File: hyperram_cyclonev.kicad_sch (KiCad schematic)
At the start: 57 parts, among them IC1 AP63205WU, IC2 TXB0108PWR, IC3 S26KL128SDABHI020, IC4 W25Q32JVSSIQ_TR, IC5 S27KL0641DABHI020, J1 ASP-122952-01, J2 HDMI_A, J3 Conn_02x10_Odd_Even, J4 Conn_02x10_Odd_Even, J5 Conn_02x06_Odd_Even, J6 Conn_02x06_Odd_Even, J7 Conn_02x06_Odd_Even, Q1 BSS138, Q2 BSS138

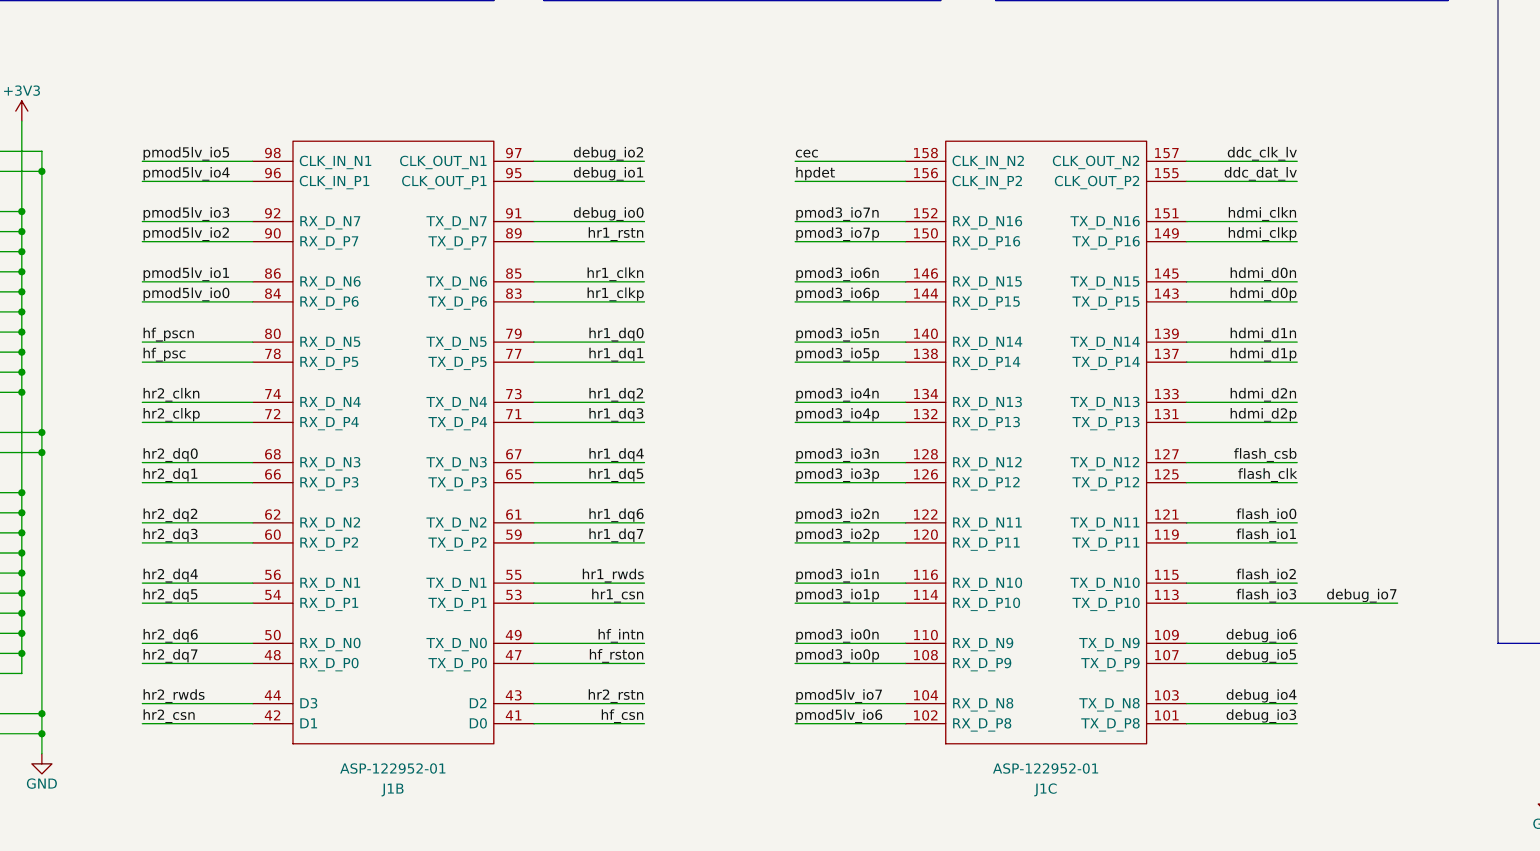
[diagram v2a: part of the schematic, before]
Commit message: Rearrange signals assignments to simplify routing.
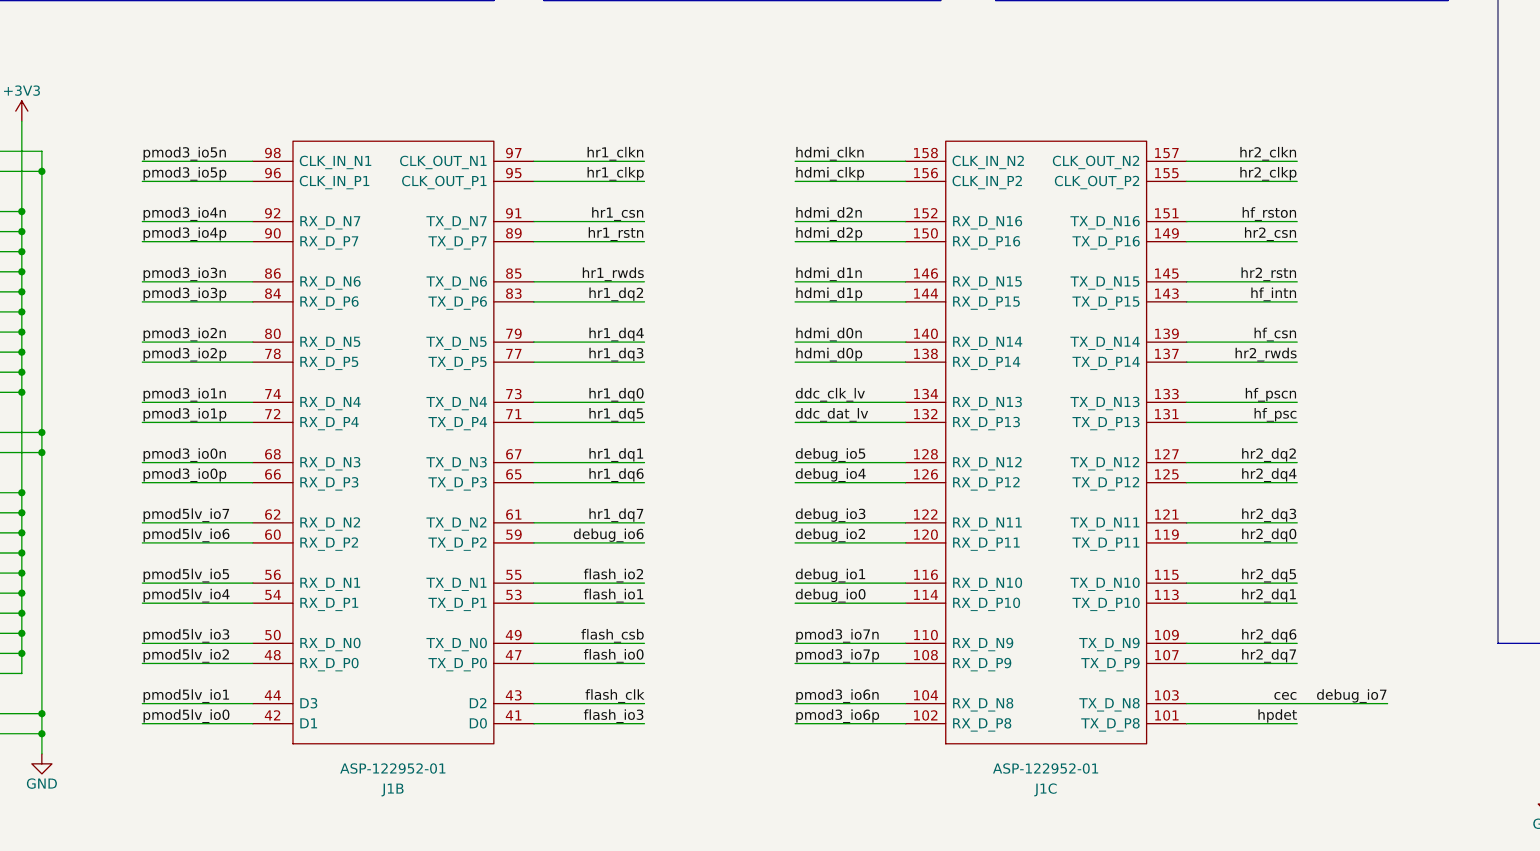
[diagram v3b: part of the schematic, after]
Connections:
- net cec: now also J1.103 (TX_D_N8), J4.3 (Pin_3); no longer J1.158 (CLK_IN_N2)
- net ddc_clk_lv: now also J1.134 (RX_D_N13); no longer J1.157 (CLK_OUT_N2)
- net ddc_dat_lv: now also J1.132 (RX_D_P13); no longer J1.155 (CLK_OUT_P2)
- net debug_io0: now also J1.114 (RX_D_P10); no longer J1.91 (TX_D_N7)
- net debug_io1: now also J1.116 (RX_D_N10); no longer J1.95 (CLK_OUT_P1)
- net debug_io2: now also J1.120 (RX_D_P11); no longer J1.97 (CLK_OUT_N1)
- net debug_io3: now also J1.122 (RX_D_N11); no longer J1.101 (TX_D_P8)
- net debug_io4: now also J1.126 (RX_D_P12); no longer J1.103 (TX_D_N8)
- net debug_io5: now also J1.128 (RX_D_N12); no longer J1.107 (TX_D_P9)
- net debug_io6: now also J1.59 (TX_D_P2); no longer J1.109 (TX_D_N9)
- net flash_clk: now also J1.43 (D2); no longer J1.125 (TX_D_P12)
- net flash_csb: now also J1.49 (TX_D_N0); no longer J1.127 (TX_D_N12)
- net flash_io0: now also J1.47 (TX_D_P0); no longer J1.121 (TX_D_N11)
- net flash_io1: now also J1.53 (TX_D_P1); no longer J1.119 (TX_D_P11)
- net flash_io2: now also J1.55 (TX_D_N1); no longer J1.115 (TX_D_N10)
- net hdmi_clkn: now also J1.158 (CLK_IN_N2); no longer J1.151 (TX_D_N16)
- net hdmi_clkp: now also J1.156 (CLK_IN_P2); no longer J1.149 (TX_D_P16)
- net hdmi_d0n: now also J1.140 (RX_D_N14); no longer J1.145 (TX_D_N15)
- net hdmi_d0p: now also J1.138 (RX_D_P14); no longer J1.143 (TX_D_P15)
- net hdmi_d1n: now also J1.146 (RX_D_N15); no longer J1.139 (TX_D_N14)
- net hdmi_d1p: now also J1.144 (RX_D_P15); no longer J1.137 (TX_D_P14)
- net hdmi_d2n: now also J1.152 (RX_D_N16); no longer J1.133 (TX_D_N13)
- net hdmi_d2p: now also J1.150 (RX_D_P16); no longer J1.131 (TX_D_P13)
- net hf_csn: now also J1.139 (TX_D_N14); no longer J1.41 (D0)
- net hf_intn: now also J1.143 (TX_D_P15); no longer J1.49 (TX_D_N0)
- net hf_psc: now also J1.131 (TX_D_P13); no longer J1.78 (RX_D_P5)
- net hf_pscn: now also J1.133 (TX_D_N13); no longer J1.80 (RX_D_N5)
- net hf_rston: now also J1.151 (TX_D_N16); no longer J1.47 (TX_D_P0)
- net hpdet: now also J1.101 (TX_D_P8); no longer J1.156 (CLK_IN_P2)
- net hr1_clkn: now also J1.97 (CLK_OUT_N1); no longer J1.85 (TX_D_N6)
- net hr1_clkp: now also J1.95 (CLK_OUT_P1); no longer J1.83 (TX_D_P6)
- net hr1_csn: now also J1.91 (TX_D_N7); no longer J1.53 (TX_D_P1)
- net hr1_dq0: now also J1.73 (TX_D_N4); no longer J1.79 (TX_D_N5)
- net hr1_dq1: now also J1.67 (TX_D_N3); no longer J1.77 (TX_D_P5)
- net hr1_dq2: now also J1.83 (TX_D_P6); no longer J1.73 (TX_D_N4)
- net hr1_dq3: now also J1.77 (TX_D_P5); no longer J1.71 (TX_D_P4)
- net hr1_dq4: now also J1.79 (TX_D_N5); no longer J1.67 (TX_D_N3)
- net hr1_dq5: now also J1.71 (TX_D_P4); no longer J1.65 (TX_D_P3)
- net hr1_dq6: now also J1.65 (TX_D_P3); no longer J1.61 (TX_D_N2)
- net hr1_dq7: now also J1.61 (TX_D_N2); no longer J1.59 (TX_D_P2)
- net hr1_rwds: now also J1.85 (TX_D_N6); no longer J1.55 (TX_D_N1)
- net hr2_clkn: now also J1.157 (CLK_OUT_N2); no longer J1.74 (RX_D_N4)
- net hr2_clkp: now also J1.155 (CLK_OUT_P2); no longer J1.72 (RX_D_P4)
- net hr2_csn: now also J1.149 (TX_D_P16); no longer J1.42 (D1)
- net hr2_dq0: now also J1.119 (TX_D_P11); no longer J1.68 (RX_D_N3)
- net hr2_dq1: now also J1.113 (TX_D_P10); no longer J1.66 (RX_D_P3)
- net hr2_dq2: now also J1.127 (TX_D_N12); no longer J1.62 (RX_D_N2)
- net hr2_dq3: now also J1.121 (TX_D_N11); no longer J1.60 (RX_D_P2)
- net hr2_dq4: now also J1.125 (TX_D_P12); no longer J1.56 (RX_D_N1)
- net hr2_dq5: now also J1.115 (TX_D_N10); no longer J1.54 (RX_D_P1)
- net hr2_dq6: now also J1.109 (TX_D_N9); no longer J1.50 (RX_D_N0)
- net hr2_dq7: now also J1.107 (TX_D_P9); no longer J1.48 (RX_D_P0)
- net hr2_rstn: now also J1.145 (TX_D_N15); no longer J1.43 (D2)
- net hr2_rwds: now also J1.137 (TX_D_P14); no longer J1.44 (D3)
- net pmod3_io0n: now also J1.68 (RX_D_N3); no longer J1.110 (RX_D_N9)
- net pmod3_io0p: now also J1.66 (RX_D_P3); no longer J1.108 (RX_D_P9)
- net pmod3_io1n: now also J1.74 (RX_D_N4); no longer J1.116 (RX_D_N10)
- net pmod3_io1p: now also J1.72 (RX_D_P4); no longer J1.114 (RX_D_P10)
- net pmod3_io2n: now also J1.80 (RX_D_N5); no longer J1.122 (RX_D_N11)
- net pmod3_io2p: now also J1.78 (RX_D_P5); no longer J1.120 (RX_D_P11)
- net pmod3_io3n: now also J1.86 (RX_D_N6); no longer J1.128 (RX_D_N12)
- net pmod3_io3p: now also J1.84 (RX_D_P6); no longer J1.126 (RX_D_P12)
- net pmod3_io4n: now also J1.92 (RX_D_N7); no longer J1.134 (RX_D_N13)
- net pmod3_io4p: now also J1.90 (RX_D_P7); no longer J1.132 (RX_D_P13)
- net pmod3_io5n: now also J1.98 (CLK_IN_N1); no longer J1.140 (RX_D_N14)
- net pmod3_io5p: now also J1.96 (CLK_IN_P1); no longer J1.138 (RX_D_P14)
- net pmod3_io6n: now also J1.104 (RX_D_N8); no longer J1.146 (RX_D_N15)
- net pmod3_io6p: now also J1.102 (RX_D_P8); no longer J1.144 (RX_D_P15)
- net pmod3_io7n: now also J1.110 (RX_D_N9); no longer J1.152 (RX_D_N16)
- net pmod3_io7p: now also J1.108 (RX_D_P9); no longer J1.150 (RX_D_P16)
- net pmod5lv_io0: now also J1.42 (D1); no longer J1.84 (RX_D_P6)
- net pmod5lv_io1: now also J1.44 (D3); no longer J1.86 (RX_D_N6)
- net pmod5lv_io2: now also J1.48 (RX_D_P0); no longer J1.90 (RX_D_P7)
- net pmod5lv_io3: now also J1.50 (RX_D_N0); no longer J1.92 (RX_D_N7)
- net pmod5lv_io4: now also J1.54 (RX_D_P1); no longer J1.96 (CLK_IN_P1)
- net pmod5lv_io5: now also J1.56 (RX_D_N1); no longer J1.98 (CLK_IN_N1)
- net pmod5lv_io6: now also J1.60 (RX_D_P2); no longer J1.102 (RX_D_P8)
- net pmod5lv_io7: now also J1.62 (RX_D_N2); no longer J1.104 (RX_D_N8)
- removed net debug_io7: IC4.7 (IO3), J1.113 (TX_D_P10), J4.3 (Pin_3)
- new net flash_io3: IC4.7 (IO3), J1.41 (D0)
